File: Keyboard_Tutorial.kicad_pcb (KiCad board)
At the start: 2 copper layers, 24 parts, among them SW1 SW_Push, U1 ATmega32U4-AU, Y1 16MHz

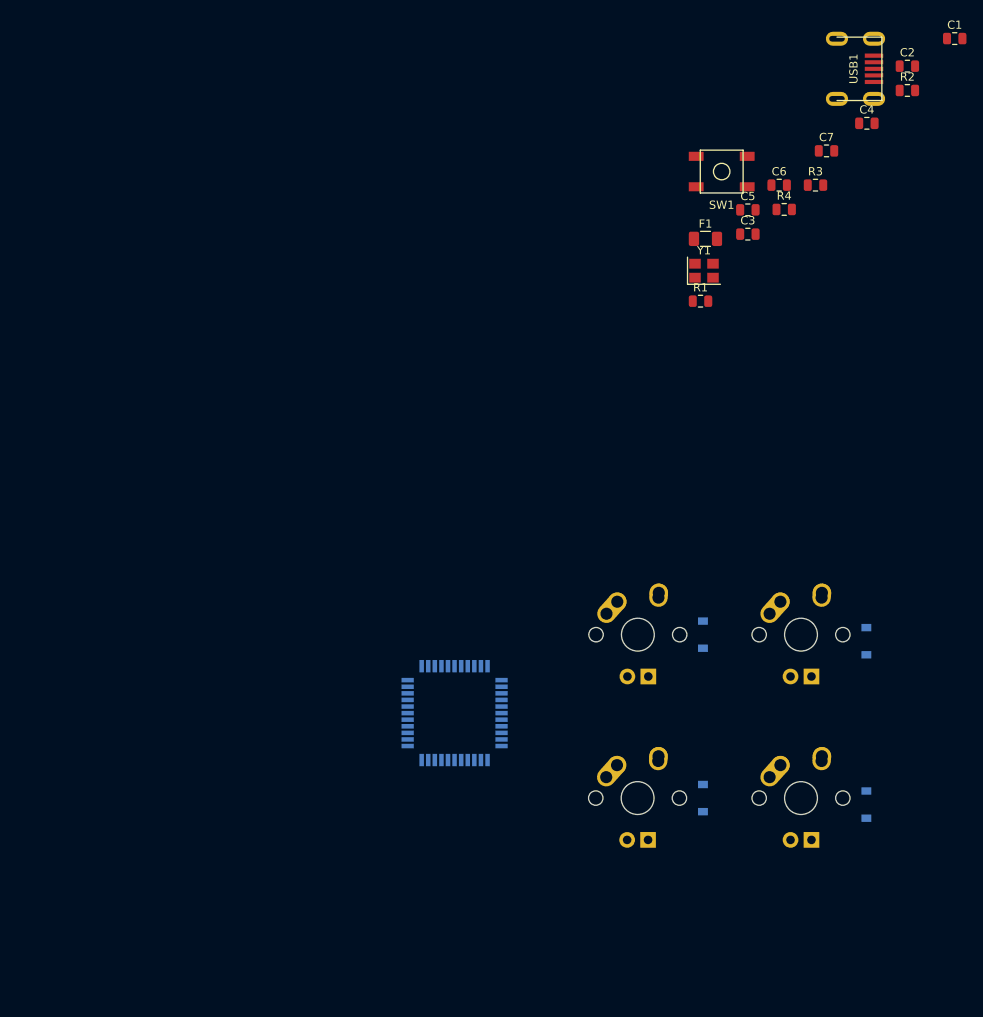
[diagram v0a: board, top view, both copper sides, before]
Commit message: Add submodules
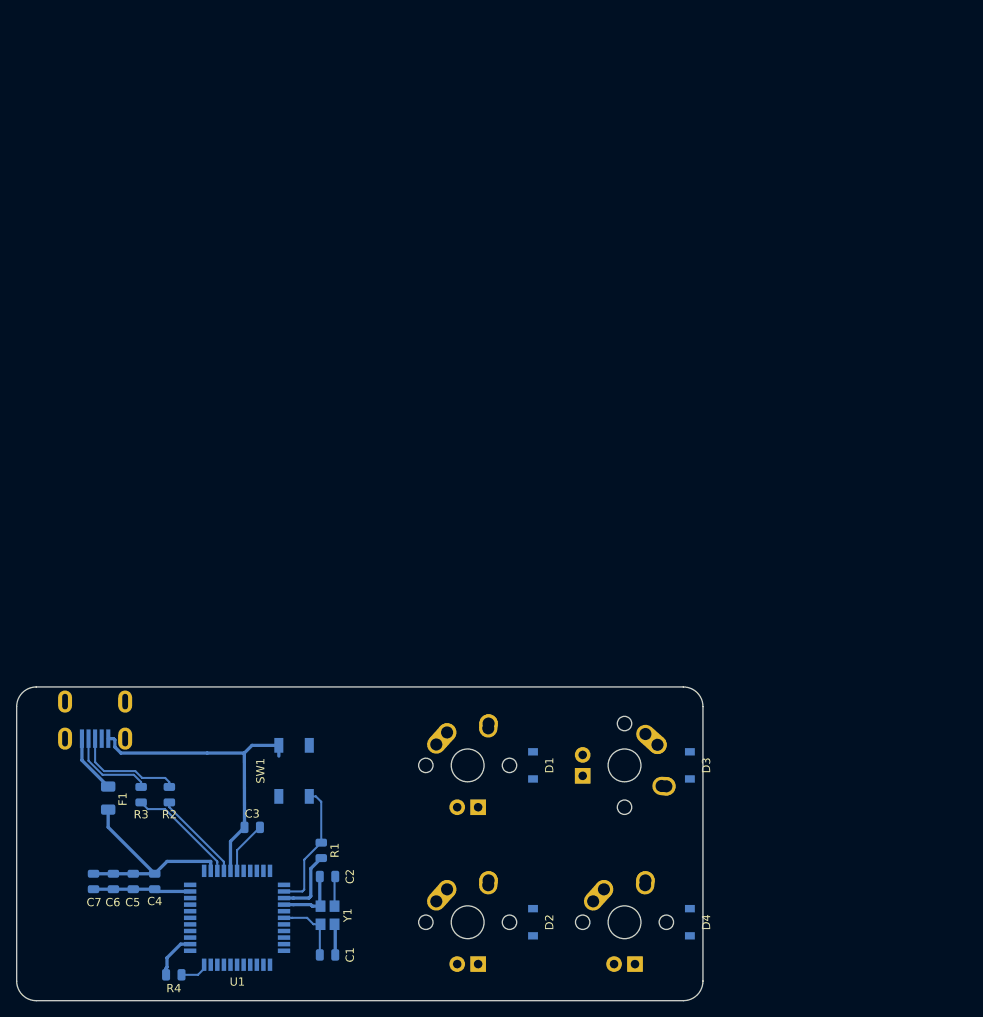
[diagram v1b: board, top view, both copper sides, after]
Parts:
- C1, C2: value 22pF -> _; moved to B.Cu
- C3: value 1uF -> _; moved to B.Cu
- C4, C5, C6: value .1uF -> _; moved to B.Cu
- C7: value 10uF -> _; moved to B.Cu
- D4: value D_Small -> _
- F1: value 500mA -> _; moved to B.Cu
- MX4: value MX-NoLED -> _
- R1, R4: value 10k -> _; moved to B.Cu
- R2, R3: value 22 -> _; moved to B.Cu
- SW1: value SW_Push -> _; moved to B.Cu
- U1: value ATmega32U4-AU -> atmega
- USB1: moved to B.Cu
- Y1: value 16MHz -> C; moved to B.Cu
- moved C1 134.9 mm to (136.2, 153.2), turned to 180 degrees
- moved C4 126.3 mm to (115.2, 144.3), turned to 270 degrees
- moved C7 125.7 mm to (107.8, 144.3), turned to 90 degrees
- moved R2 123.9 mm to (117.0, 133.7), turned to 90 degrees
- moved C2 121.0 mm to (136.2, 143.7), turned to 180 degrees
- moved R4 118.9 mm to (117.5, 155.6)
- moved USB1 118.4 mm to (108.0, 122.4), turned to 270 degrees
- moved C6 117.0 mm to (110.2, 144.3), turned to 270 degrees
- moved C5 110.6 mm to (112.6, 144.3), turned to 270 degrees
- moved R3 110.4 mm to (113.5, 133.7), turned to 90 degrees
- moved F1 99.4 mm to (109.5, 134.1), turned to 90 degrees
- moved C3 93.9 mm to (127.0, 137.7), turned to 180 degrees
- moved Y1 90.6 mm to (136.2, 148.4), turned to 90 degrees
- moved SW1 89.4 mm to (132.1, 130.8), turned to 90 degrees
- moved R1 81.1 mm to (135.4, 140.5), turned to 90 degrees
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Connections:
- D2 pad 1: ROW0 -> ROW1
- D3 pad 1: ROW1 -> ROW0
- MX2 pad 1: COL1 -> COL0
- MX3 pad 1: COL0 -> COL1
- Y1 pad 1: GND -> Net-(C1-Pad2)
- Y1 pad 2: Net-(C2-Pad1) -> GND
- Y1 pad 3: Net-(C1-Pad2) -> Net-(C2-Pad1)
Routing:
- net GND: track 0.00 -> 68.0 mm
- net +5V: track 0.00 -> 34.6 mm
- net Net-(R1-Pad2): track 0.00 -> 15.8 mm
- net D+: track 0.00 -> 13.5 mm
- net Net-(R3-Pad1): track 0.00 -> 13.4 mm
- net Net-(R2-Pad1): track 0.00 -> 11.1 mm
- net D-: track 0.00 -> 10.7 mm
- net Net-(C1-Pad2): track 0.00 -> 8.52 mm
- net VCC: track 0.00 -> 7.14 mm
- net Net-(C3-Pad1): track 0.00 -> 6.44 mm
- net Net-(C2-Pad1): track 0.00 -> 3.64 mm
- net Net-(R4-Pad2): track 0.00 -> 3.53 mm
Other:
- board outline added: 83.3 x 38.1 mm
- net class Power added: clearance 0.2, trace_width 0.4, via_dia 0.8, via_drill 0.4
